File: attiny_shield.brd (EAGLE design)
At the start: 100 x 80 mm, 10 parts, among them IC1 TINY13-20PU

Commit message: added reset switch
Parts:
- added ARDUINO_RESET: MOMENTARY-SWITCH-SPST-SMD-4.5MM, SparkFun-Switches:TACTILE_SWITCH_SMD_4.5MM
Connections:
- net GND: now also ARDUINO_RESET.1, ARDUINO_RESET.4
- net N$10: now also ARDUINO_RESET.2, ARDUINO_RESET.3
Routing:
- net GND: track 114.4 -> 124.4 mm
- net N$10: track 50.5 -> 54.6 mm
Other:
- board text added: "Arduino Reset"
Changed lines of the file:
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@@
 <layer number="27" name="tValues" color="7" fill="1" visible="yes" active="yes"/>
 <layer number="28" name="bValues" color="7" fill="1" visible="yes" active="yes"/>
-<layer number="29" name="tStop" color="7" fill="3" visible="no" active="yes"/>
-<layer number="30" name="bStop" color="7" fill="6" visible="no" active="yes"/>
-<layer number="31" name="tCream" color="7" fill="4" visible="no" active="yes"/>
-<layer number="32" name="bCream" color="7" fill="5" visible="no" active="yes"/>
-<layer number="33" name="tFinish" color="6" fill="3" visible="no" active="yes"/>
-<layer number="34" name="bFinish" color="6" fill="6" visible="no" active="yes"/>
-<layer number="35" name="tGlue" color="7" fill="4" visible="no" active="yes"/>
-<layer number="36" name="bGlue" color="7" fill="5" visible="no" active="yes"/>
-<layer number="37" name="tTest" color="7" fill="1" visible="no" active="yes"/>
-<layer number="38" name="bTest" color="7" fill="1" visible="no" active="yes"/>
+<layer number="29" name="tStop" color="7" fill="3" visible="yes" active="yes"/>
+<layer number="30" name="bStop" color="7" fill="6" visible="yes" active="yes"/>
+<layer number="31" name="tCream" color="7" fill="4" visible="yes" active="yes"/>
+<layer number="32" name="bCream" color="7" fill="5" visible="yes" active="yes"/>
+<layer number="33" name="tFinish" color="6" fill="3" visible="yes" active="yes"/>
+<layer number="34" name="bFinish" color="6" fill="6" visible="yes" active="yes"/>
+<layer number="35" name="tGlue" color="7" fill="4" visible="yes" active="yes"/>
+<layer number="36" name="bGlue" color="7" fill="5" visible="yes" active="yes"/>
+<layer number="37" name="tTest" color="7" fill="1" visible="yes" active="yes"/>
+<layer number="38" name="bTest" color="7" fill="1" visible="yes" active="yes"/>
 <layer number="39" name="tKeepout" color="4" fill="11" visible="yes" active="yes"/>
 <layer number="40" name="bKeepout" color="1" fill="11" visible="yes" active="yes"/>
@@
 <layer number="42" name="bRestrict" color="1" fill="10" visible="yes" active="yes"/>
 <layer number="43" name="vRestrict" color="2" fill="10" visible="yes" active="yes"/>
-<layer number="44" name="Drills" color="7" fill="1" visible="no" active="yes"/>
-<layer number="45" name="Holes" color="7" fill="1" visible="no" active="yes"/>
-<layer number="46" name="Milling" color="3" fill="1" visible="no" active="yes"/>
-<layer number="47" name="Measures" color="7" fill="1" visible="no" active="yes"/>
+<layer number="44" name="Drills" color="7" fill="1" visible="yes" active="yes"/>
+<layer number="45" name="Holes" color="7" fill="1" visible="yes" active="yes"/>
+<layer number="46" name="Milling" color="3" fill="1" visible="yes" active="yes"/>
+<layer number="47" name="Measures" color="7" fill="1" visible="yes" active="yes"/>
 <layer number="48" name="Document" color="7" fill="1" visible="yes" active="yes"/>
 <layer number="49" name="Reference" color="7" fill="1" visible="yes" active="yes"/>
@@
 <text x="39.37" y="32.004" size="2.1844" layer="25" rot="MR0">TinyShield</text>
 <text x="39.37" y="29.718" size="1.27" layer="25" rot="MR0">joshua noble 2018</text>
+<text x="28.194" y="18.796" size="1.27" layer="25" rot="R90">Arduino Reset</text>
 </plain>
 <attributes>
@@
 <attribute name="PROD_ID" value="CAP-11330" x="31.75" y="31.75" size="1.778" layer="27" display="off"/>
 </element>
+<element name="ARDUINO_RESET" library="SparkFun-Switches" package="TACTILE_SWITCH_SMD_4.5MM" value="MOMENTARY-SWITCH-SPST-SMD-4.5MM" x="31.496" y="23.876" smashed="yes">
+<attribute name="PROD_ID" value="SWCH-09213" x="31.496" y="23.876" size="1.778" layer="27" display="off"/>
+</element>
 </elements>
 <signals>
@@
 <wire x1="48.895" y1="66.04" x2="49.276" y2="66.04" width="0.1524" layer="16"/>
 <wire x1="33.655" y1="31.115" x2="33.02" y2="31.75" width="0.2032" layer="1"/>
-<wire x1="80.645" y1="31.115" x2="33.655" y2="31.115" width="0.2032" layer="1"/>
+<wire x1="33.782" y1="31.115" x2="80.645" y2="31.115" width="0.2032" layer="1"/>
+<wire x1="33.782" y1="31.115" x2="33.655" y2="31.115" width="0.2032" layer="1"/>
 <wire x1="82.55" y1="33.02" x2="80.645" y2="31.115" width="0.2032" layer="1"/>
 <wire x1="33.02" y1="31.75" x2="32.65" y2="31.75" width="0.1524" layer="1"/>
@@
 <wire x1="80.645" y1="40.005" x2="53.975" y2="40.005" width="0.2032" layer="16"/>
 <wire x1="82.55" y1="38.1" x2="80.645" y2="40.005" width="0.2032" layer="16"/>
+<contactref element="ARDUINO_RESET" pad="1"/>
+<contactref element="ARDUINO_RESET" pad="4"/>
+<wire x1="33.721" y1="25.626" x2="33.721" y2="31.054" width="0.1524" layer="1"/>
+<wire x1="33.721" y1="31.054" x2="33.782" y2="31.115" width="0.1524" layer="1"/>
+<wire x1="29.271" y1="25.626" x2="33.721" y2="25.626" width="0.1524" layer="1"/>
 </signal>
 <signal name="VIN">
@@
 <wire x1="29.845" y1="43.815" x2="31.115" y2="43.815" width="0.2032" layer="1"/>
 <wire x1="27.94" y1="41.91" x2="29.845" y2="43.815" width="0.2032" layer="1"/>
-<wire x1="52.705" y1="20.955" x2="36.195" y2="20.955" width="0.2032" layer="1"/>
-<wire x1="36.195" y1="20.955" x2="27.94" y2="29.21" width="0.2032" layer="1"/>
-<wire x1="27.94" y1="29.21" x2="27.94" y2="41.91" width="0.2032" layer="1"/>
+<wire x1="52.705" y1="20.955" x2="34.925" y2="20.955" width="0.2032" layer="1"/>
+<wire x1="34.925" y1="20.955" x2="34.036" y2="21.844" width="0.2032" layer="1"/>
+<wire x1="34.036" y1="21.844" x2="33.782" y2="22.098" width="0.2032" layer="1"/>
+<wire x1="34.036" y1="21.844" x2="29.718" y2="21.844" width="0.2032" layer="1"/>
+<wire x1="29.591" y1="21.971" x2="29.718" y2="21.844" width="0.2032" layer="1"/>
+<wire x1="29.591" y1="21.971" x2="27.94" y2="23.622" width="0.2032" layer="1"/>
+<wire x1="27.94" y1="23.622" x2="27.94" y2="41.91" width="0.2032" layer="1"/>
 <wire x1="55.88" y1="17.78" x2="52.705" y2="20.955" width="0.2032" layer="1"/>
 <wire x1="31.75" y1="44.45" x2="31.75" y2="44.735" width="0.1524" layer="1"/>
+<contactref element="ARDUINO_RESET" pad="3"/>
+<contactref element="ARDUINO_RESET" pad="2"/>
+<wire x1="29.271" y1="22.126" x2="29.436" y2="22.126" width="0.1524" layer="1"/>
+<wire x1="29.436" y1="22.126" x2="29.591" y2="21.971" width="0.1524" layer="1"/>
+<wire x1="33.782" y1="22.098" x2="33.749" y2="22.098" width="0.1524" layer="1"/>
+<wire x1="33.749" y1="22.098" x2="33.721" y2="22.126" width="0.1524" layer="1"/>
 </signal>
 <signal name="VCC">

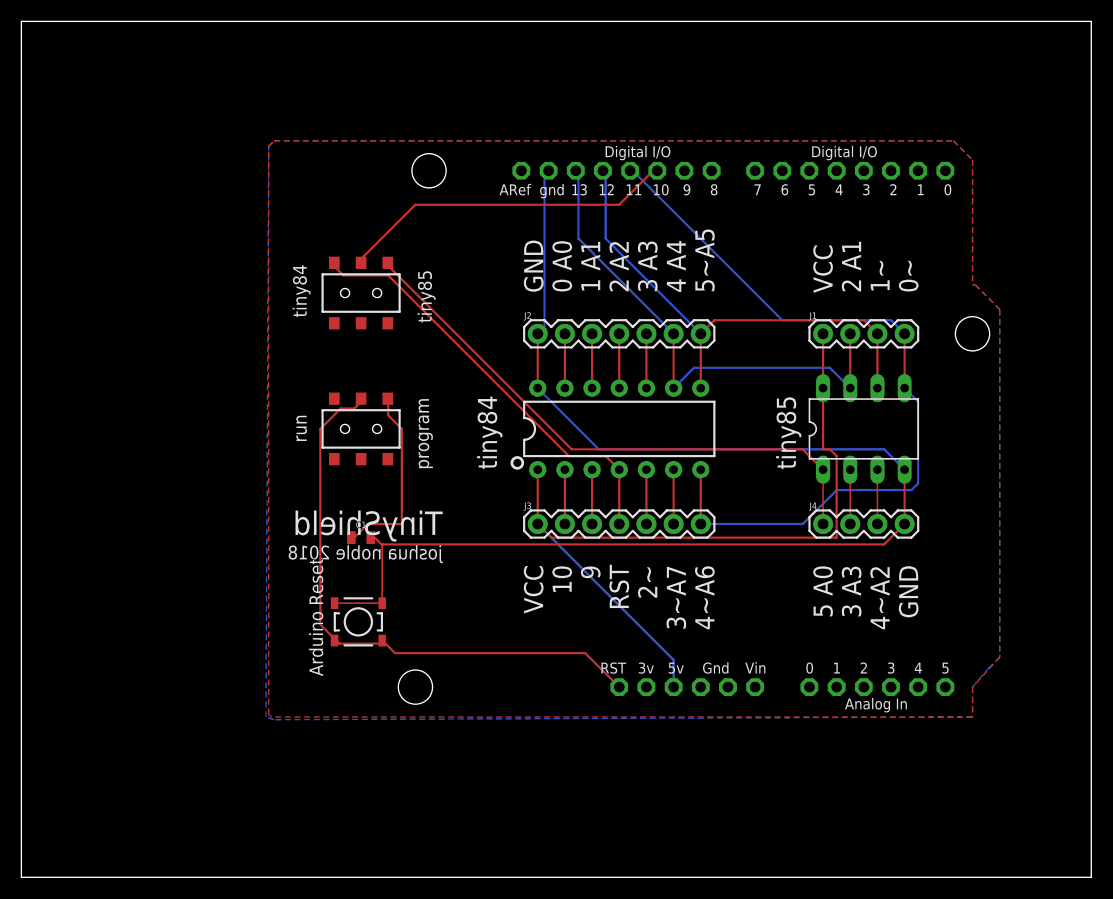
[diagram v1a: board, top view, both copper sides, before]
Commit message: independent resets
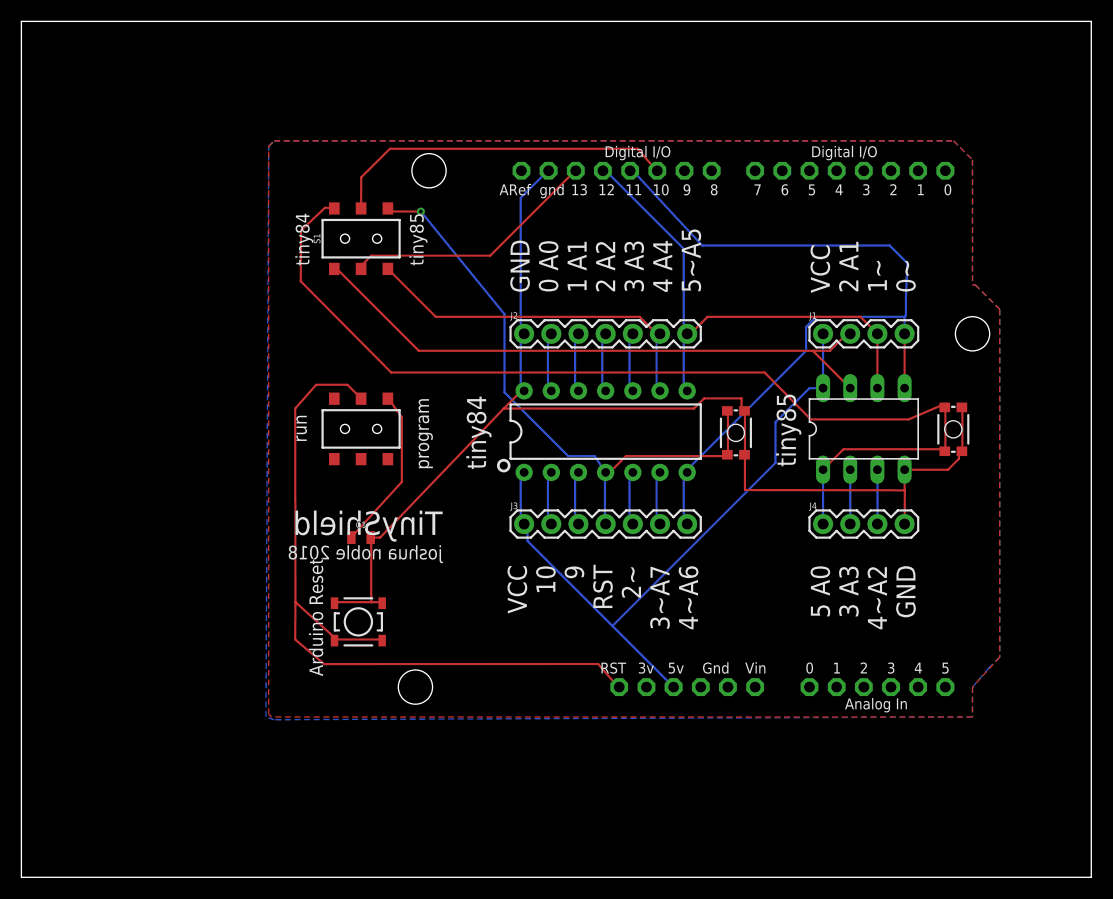
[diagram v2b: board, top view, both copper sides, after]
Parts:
- removed 85_V_84: (no value), SparkFun-Switches:SWITCH_DPDT_SMD_AYZ0202
- added S1: (no value), SparkFun-Switches:SWITCH_DPDT_SMD_AYZ0202
- added TINY_RESET, TINY_RESET1: MOMENTARY-SWITCH-SPST-SMD-4.6X2.8MM, SparkFun-Switches:TACTILE_SWITCH_SMD_4.6X2.8MM
- moved U$1 1.30 mm to (54.6, 41.7)
- moved J2 1.27 mm to (47.0, 50.8)
- moved J3 1.27 mm to (47.0, 33.0)
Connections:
- removed net N$1: IC1.7, J1.2, J2.6, U$1.9, U$2.D13
- new net ARD_SCK: S1.5, U$2.D13
- new net TINY84_SCK: J2.6, S1.6, U$1.9
- new net TINY85_SCK: IC1.7, J1.2, S1.4
- net GND: now also TINY_RESET.1, TINY_RESET.2, TINY_RESET1.1, TINY_RESET1.2
- net TINY84_RESET: now also S1.3, TINY_RESET1.3, TINY_RESET1.4; no longer 85_V_84.1
- net TINY85_RESET: now also S1.1, TINY_RESET.3, TINY_RESET.4; no longer 85_V_84.3
- net TINY_RESET: now also S1.2; no longer 85_V_84.2
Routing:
- net TINY85_SCK: track 0.00 -> 57.0 mm
- net N$1: track 47.4 -> 0.00 mm
- net TINY85_RESET: track 53.9 -> 96.1 mm
- net TINY84_SCK: track 0.00 -> 33.5 mm
- net ARD_SCK: track 0.00 -> 24.0 mm
- net TINY84_RESET: track 39.9 -> 57.1 mm, vias 0 -> 1
- net N$10: track 54.6 -> 71.6 mm
- net VCC: track 74.0 -> 62.3 mm
- net GND: track 124.4 -> 114.9 mm
- net N$9: track 17.5 -> 15.7 mm
- net 84_5: track 46.9 -> 48.6 mm
- net TINY_RESET: track 31.5 -> 32.6 mm
- net 84_6: track 73.4 -> 74.3 mm
- net N$14: track 5.08 -> 5.60 mm
- net 84_1: track 5.08 -> 5.60 mm
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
